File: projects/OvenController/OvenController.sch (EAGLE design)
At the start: 33 parts, among them IC1 ESP32-WROOM-32U, J5 UJ2-MIBH2-4-SMT-TR, K1 CPC2030N, K2 CPC2030N, K3 CPC2030N, Q2 MBT3904DW1T1, U1 LTV-816_OPTO_ISOLATOR", U3 AP2112K-3.3V, U4 CP2102N

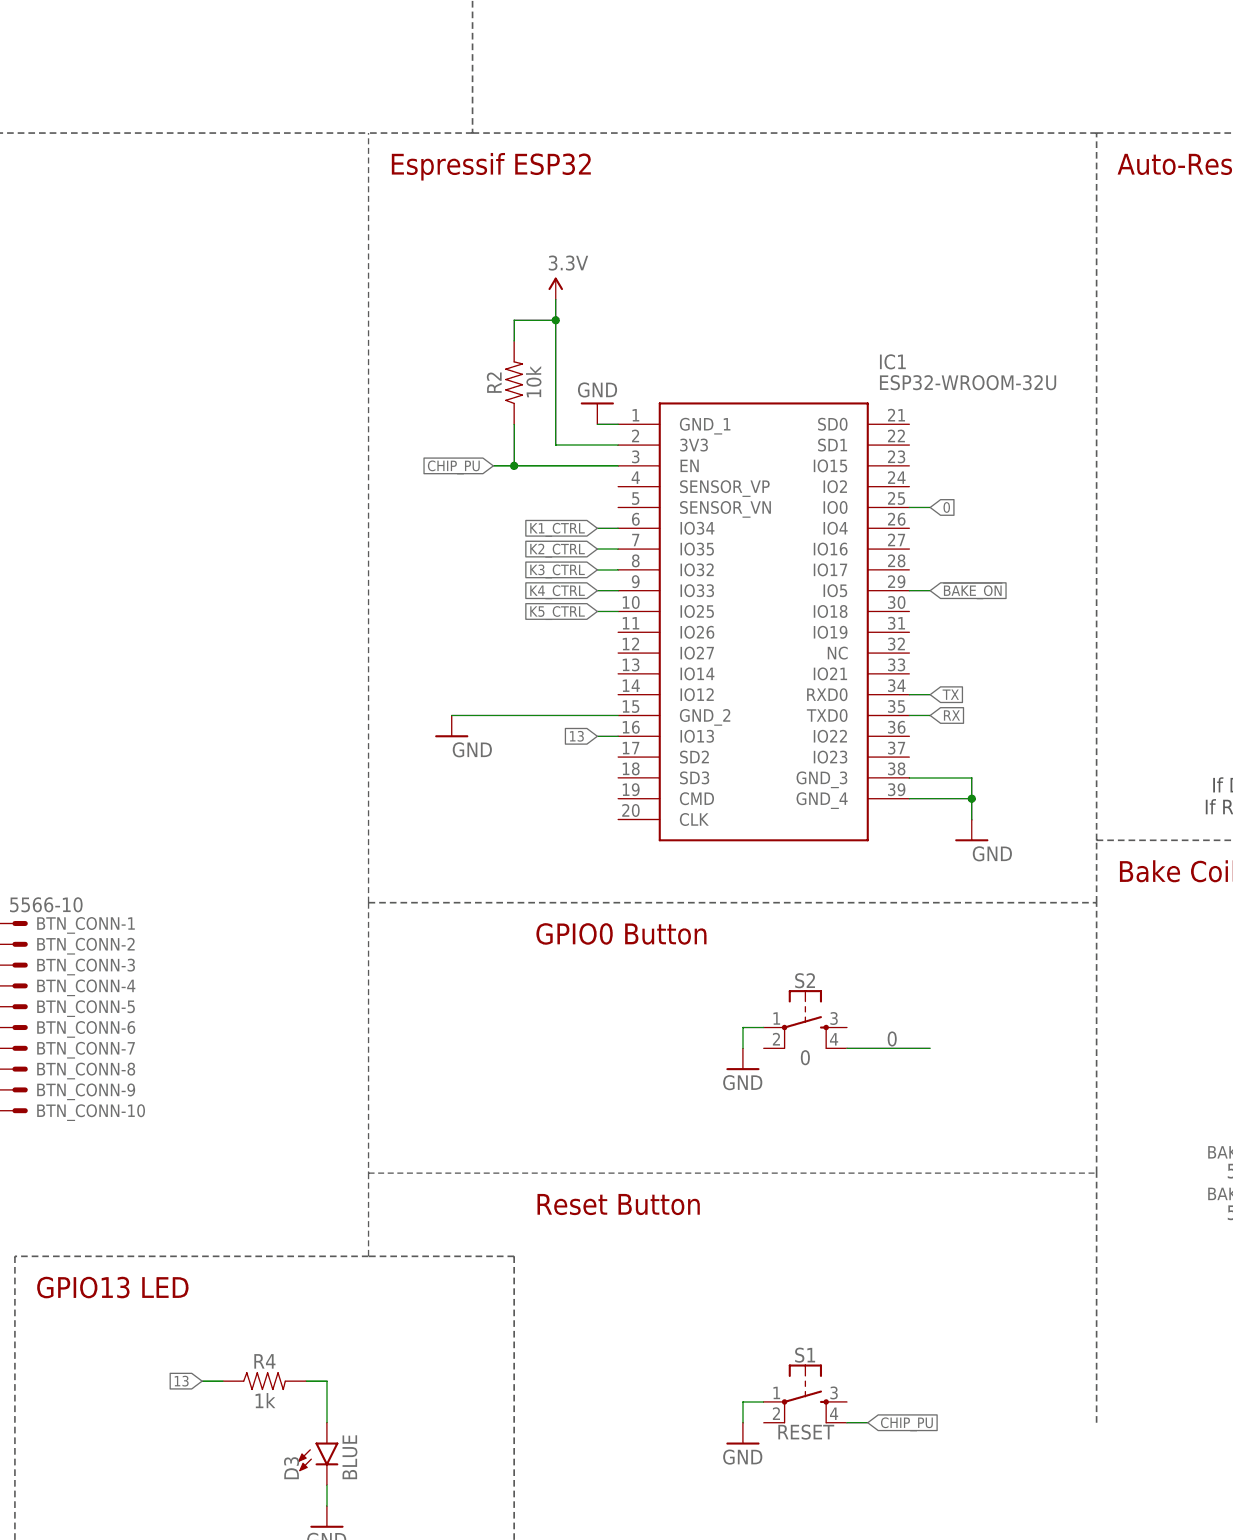
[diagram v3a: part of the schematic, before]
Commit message: Oven Controller v1.1
Added JTAG header.
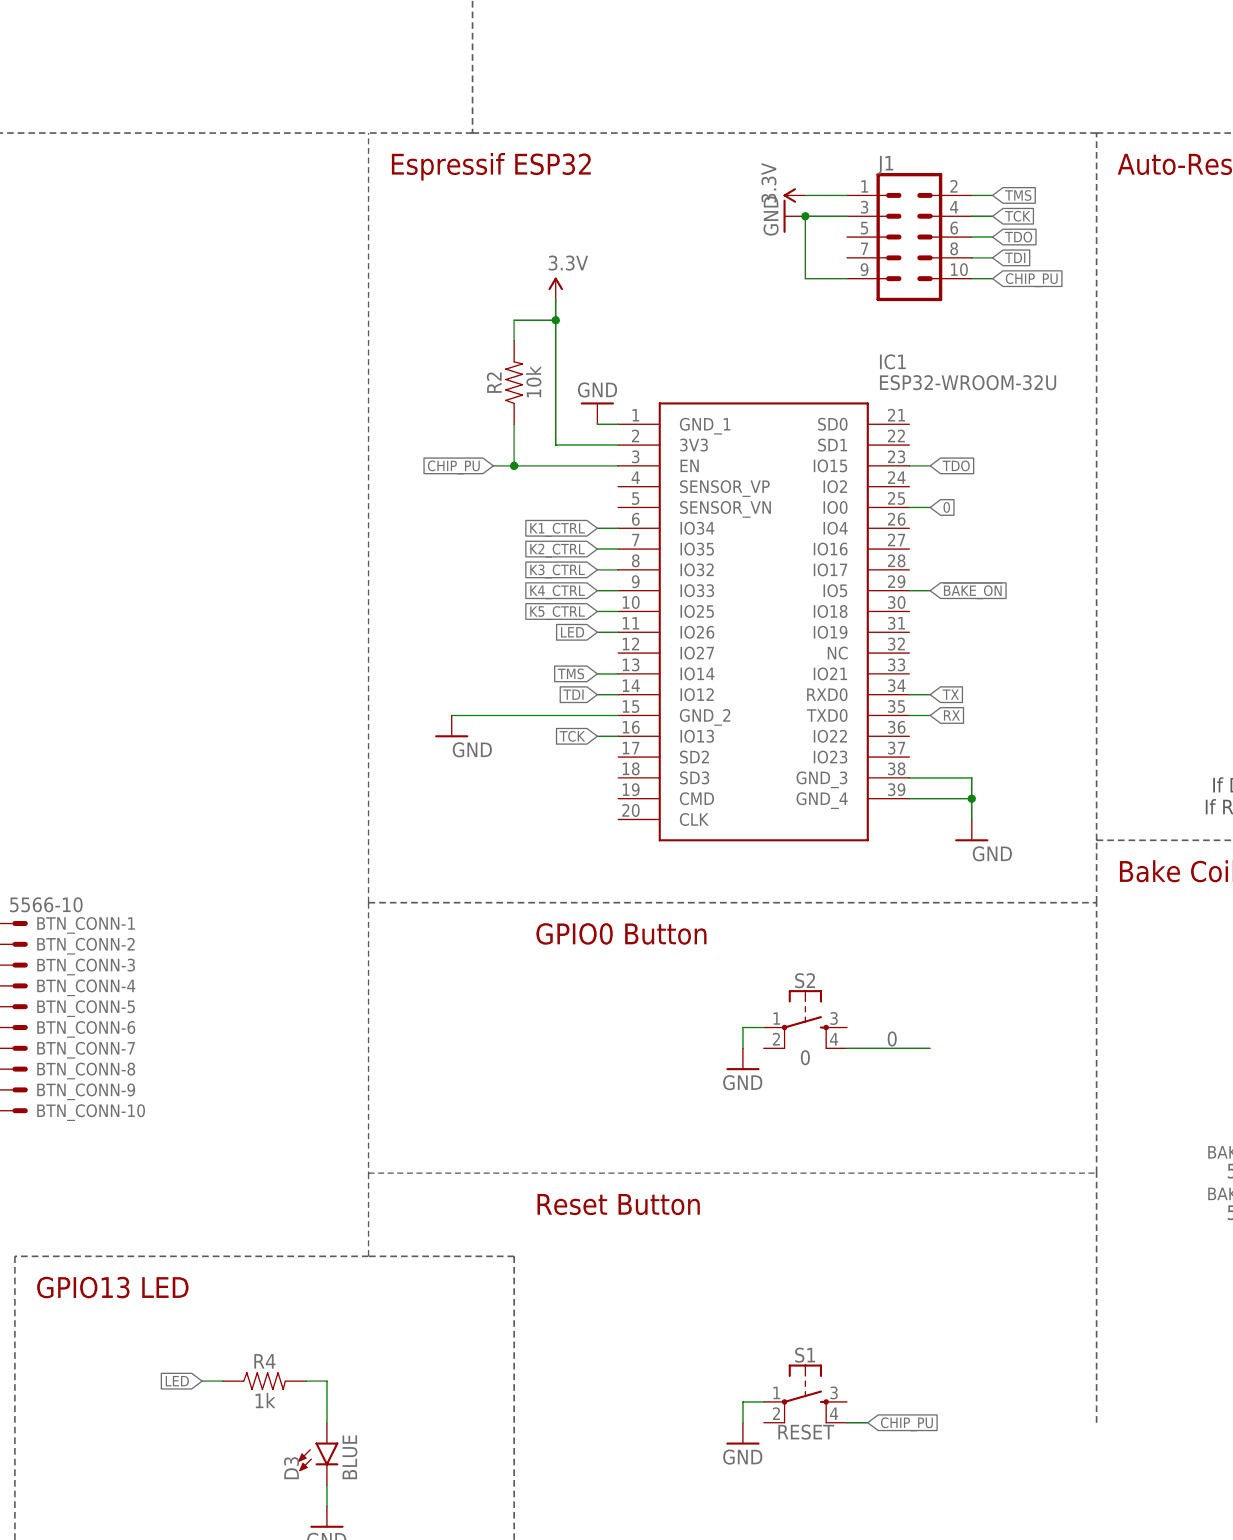
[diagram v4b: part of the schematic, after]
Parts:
- added J1: (no value), SparkFun-Connectors:CONN_05X2PTH
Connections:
- removed net 13: IC1.IO13, R4.1
- new net LED: IC1.IO26, R4.1
- new net TCK: IC1.IO13, J1.4
- new net TDI: IC1.IO12, J1.8
- new net TDO: IC1.IO15, J1.6
- new net TMS: IC1.IO14, J1.2
- net 3.3V: now also J1.1
- net CHIP_PU: now also J1.10
- net GND: now also J1.3, J1.9
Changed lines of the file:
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@@
 <part name="GND9" library="SparkFun-Aesthetics" deviceset="GND" device=""/>
 <part name="R13" library="rcl" library_urn="urn:adsk.eagle:library:334" deviceset="R-US_" device="R1210W" package3d_urn="urn:adsk.eagle:package:23541/2" value="300"/>
+<part name="J1" library="SparkFun-Connectors" deviceset="CONN_05X2" device="PTH"/>
+<part name="SUPPLY1" library="SparkFun-Aesthetics" deviceset="3.3V" device=""/>
+<part name="GND11" library="SparkFun-Aesthetics" deviceset="GND" device=""/>
 </parts>
 <sheets>
@@
 <attribute name="NAME" x="363.22" y="67.056" size="1.778" layer="95" font="vector" rot="R180" align="bottom-center"/>
 </instance>
+<instance part="J1" gate="G$1" x="307.34" y="180.34" smashed="yes">
+<attribute name="VALUE" x="303.53" y="170.434" size="1.778" layer="96" font="vector"/>
+<attribute name="NAME" x="303.53" y="188.468" size="1.778" layer="95" font="vector"/>
+</instance>
+<instance part="SUPPLY1" gate="G$1" x="294.64" y="185.42" smashed="yes" rot="R90">
+<attribute name="VALUE" x="291.084" y="184.404" size="1.778" layer="96" rot="R90"/>
+</instance>
+<instance part="GND11" gate="1" x="292.1" y="182.88" smashed="yes" rot="R270">
+<attribute name="VALUE" x="289.56" y="185.42" size="1.778" layer="96" rot="R270"/>
+</instance>
 </instances>
 <busses>
@@
 <wire x1="396.24" y1="83.82" x2="396.24" y2="86.36" width="0.1524" layer="91"/>
 </segment>
+<segment>
+<pinref part="J1" gate="G$1" pin="1"/>
+<wire x1="299.72" y1="185.42" x2="294.64" y2="185.42" width="0.1524" layer="91"/>
+<pinref part="SUPPLY1" gate="G$1" pin="3.3V"/>
+</segment>
 </net>
 <net name="CHIP_PU" class="0">
@@
 <pinref part="S1" gate="G$1" pin="4"/>
 <wire x1="299.72" y1="35.56" x2="302.26" y2="35.56" width="0.1524" layer="91"/>
+</segment>
+<segment>
+<pinref part="J1" gate="G$1" pin="10"/>
+<wire x1="314.96" y1="175.26" x2="317.5" y2="175.26" width="0.1524" layer="91"/>
+<label x="317.5" y="175.26" size="1.27" layer="95" xref="yes"/>
 </segment>
 </net>
@@
 <pinref part="R12" gate="G$1" pin="1"/>
 <wire x1="5.08" y1="121.92" x2="5.08" y2="111.76" width="0.1524" layer="91"/>
+</segment>
+<segment>
+<pinref part="J1" gate="G$1" pin="3"/>
+<wire x1="299.72" y1="182.88" x2="294.64" y2="182.88" width="0.1524" layer="91"/>
+<pinref part="GND11" gate="1" pin="GND"/>
+<pinref part="J1" gate="G$1" pin="9"/>
+<wire x1="299.72" y1="175.26" x2="294.64" y2="175.26" width="0.1524" layer="91"/>
+<wire x1="294.64" y1="175.26" x2="294.64" y2="182.88" width="0.1524" layer="91"/>
+<junction x="294.64" y="182.88"/>
 </segment>
 </net>
@@
 </segment>
 </net>
-<net name="13" class="0">
-<segment>
-<pinref part="R4" gate="G$1" pin="1"/>
-<wire x1="223.52" y1="40.64" x2="220.98" y2="40.64" width="0.1524" layer="91"/>
-<label x="220.98" y="40.64" size="1.27" layer="95" rot="R180" xref="yes"/>
-</segment>
+<net name="TCK" class="0">
 <segment>
 <pinref part="IC1" gate="G$1" pin="IO13"/>
 <wire x1="271.78" y1="119.38" x2="269.24" y2="119.38" width="0.1524" layer="91"/>
 <label x="269.24" y="119.38" size="1.27" layer="95" rot="R180" xref="yes"/>
+</segment>
+<segment>
+<pinref part="J1" gate="G$1" pin="4"/>
+<wire x1="314.96" y1="182.88" x2="317.5" y2="182.88" width="0.1524" layer="91"/>
+<label x="317.5" y="182.88" size="1.27" layer="95" xref="yes"/>
 </segment>
 </net>
@@
 </segment>
 </net>
+<net name="TMS" class="0">
+<segment>
+<pinref part="IC1" gate="G$1" pin="IO14"/>
+<wire x1="271.78" y1="127" x2="269.24" y2="127" width="0.1524" layer="91"/>
+<label x="269.24" y="127" size="1.27" layer="95" rot="R180" xref="yes"/>
+</segment>
+<segment>
+<pinref part="J1" gate="G$1" pin="2"/>
+<wire x1="314.96" y1="185.42" x2="317.5" y2="185.42" width="0.1524" layer="91"/>
+<label x="317.5" y="185.42" size="1.27" layer="95" xref="yes"/>
+</segment>
+</net>
+<net name="TDI" class="0">
+<segment>
+<pinref part="IC1" gate="G$1" pin="IO12"/>
+<wire x1="271.78" y1="124.46" x2="269.24" y2="124.46" width="0.1524" layer="91"/>
+<label x="269.24" y="124.46" size="1.27" layer="95" rot="R180" xref="yes"/>
+</segment>
+<segment>
+<pinref part="J1" gate="G$1" pin="8"/>
+<wire x1="314.96" y1="177.8" x2="317.5" y2="177.8" width="0.1524" layer="91"/>
+<label x="317.5" y="177.8" size="1.27" layer="95" xref="yes"/>
+</segment>
+</net>
+<net name="TDO" class="0">
+<segment>
+<pinref part="IC1" gate="G$1" pin="IO15"/>
+<wire x1="307.34" y1="152.4" x2="309.88" y2="152.4" width="0.1524" layer="91"/>
+<label x="309.88" y="152.4" size="1.27" layer="95" xref="yes"/>
+</segment>
+<segment>
+<pinref part="J1" gate="G$1" pin="6"/>
+<wire x1="314.96" y1="180.34" x2="317.5" y2="180.34" width="0.1524" layer="91"/>
+<label x="317.5" y="180.34" size="1.27" layer="95" xref="yes"/>
+</segment>
+</net>
+<net name="LED" class="0">
+<segment>
+<pinref part="IC1" gate="G$1" pin="IO26"/>
+<wire x1="271.78" y1="132.08" x2="269.24" y2="132.08" width="0.1524" layer="91"/>
+<label x="269.24" y="132.08" size="1.27" layer="95" rot="R180" xref="yes"/>
+</segment>
+<segment>
+<pinref part="R4" gate="G$1" pin="1"/>
+<wire x1="223.52" y1="40.64" x2="220.98" y2="40.64" width="0.1524" layer="91"/>
+<label x="220.98" y="40.64" size="1.27" layer="95" rot="R180" xref="yes"/>
+</segment>
+</net>

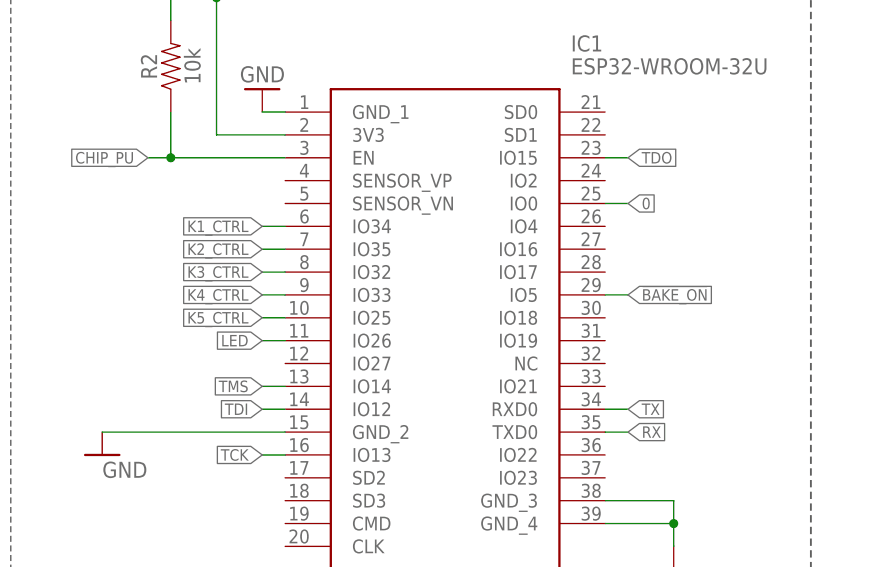
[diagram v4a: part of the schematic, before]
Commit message: Schematic revisions based on build. Layout needs update.
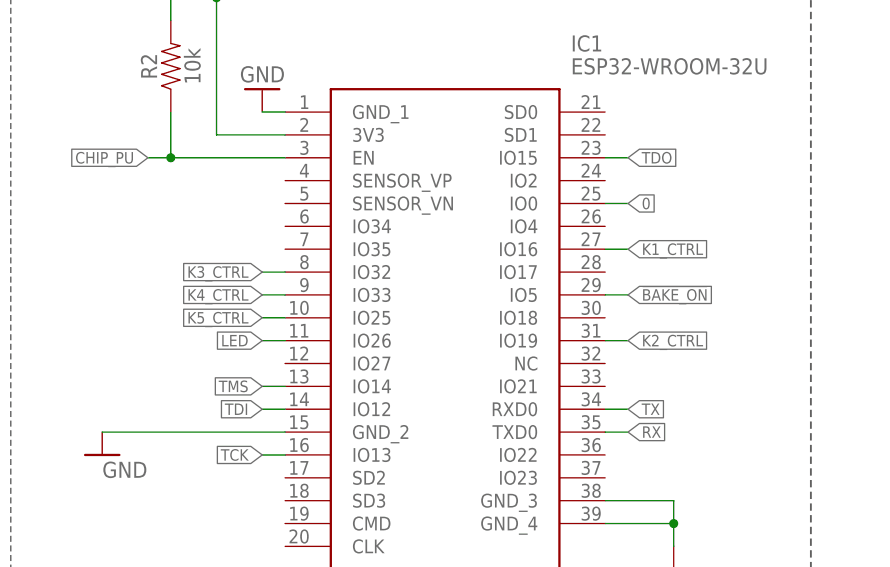
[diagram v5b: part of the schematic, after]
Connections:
- net K1_CTRL: now also IC1.IO16; no longer IC1.IO34
- net K2_CTRL: now also IC1.IO19; no longer IC1.IO35
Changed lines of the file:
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@@
 <net name="K1_CTRL" class="0">
-<segment>
-<pinref part="IC1" gate="G$1" pin="IO34"/>
-<wire x1="271.78" y1="144.78" x2="269.24" y2="144.78" width="0.1524" layer="91"/>
-<label x="269.24" y="144.78" size="1.27" layer="95" rot="R180" xref="yes"/>
-</segment>
 <segment>
 <pinref part="K1" gate="G$1" pin="CONTROL_+_1"/>
@@
 <label x="25.4" y="172.72" size="1.27" layer="95" rot="R180" xref="yes"/>
 </segment>
+<segment>
+<pinref part="IC1" gate="G$1" pin="IO16"/>
+<wire x1="307.34" y1="142.24" x2="309.88" y2="142.24" width="0.1524" layer="91"/>
+<label x="309.88" y="142.24" size="1.27" layer="95" xref="yes"/>
+</segment>
 </net>
 <net name="K2_CTRL" class="0">
-<segment>
-<pinref part="IC1" gate="G$1" pin="IO35"/>
-<wire x1="271.78" y1="142.24" x2="269.24" y2="142.24" width="0.1524" layer="91"/>
-<label x="269.24" y="142.24" size="1.27" layer="95" rot="R180" xref="yes"/>
-</segment>
 <segment>
 <pinref part="K1" gate="G$1" pin="CONTROL_+_2"/>
@@
 <label x="25.4" y="167.64" size="1.27" layer="95" rot="R180" xref="yes"/>
 </segment>
+<segment>
+<pinref part="IC1" gate="G$1" pin="IO19"/>
+<wire x1="307.34" y1="132.08" x2="309.88" y2="132.08" width="0.1524" layer="91"/>
+<label x="309.88" y="132.08" size="1.27" layer="95" xref="yes"/>
+</segment>
 </net>
